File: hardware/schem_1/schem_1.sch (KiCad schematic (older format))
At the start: 37 parts, among them J1 OV7670_Conn_01x24_MountingPin, J2 Micro_SD_Card, J3 FRONT_PCB_CONNECTOR, J4 BG300-04-X-X-A_REVC, J6 BACK_PCB_CONNECTOR, SW1 BTN_BOOT, SW2 ESP32_RESET, U1 ESP32-WROVER-E-JC

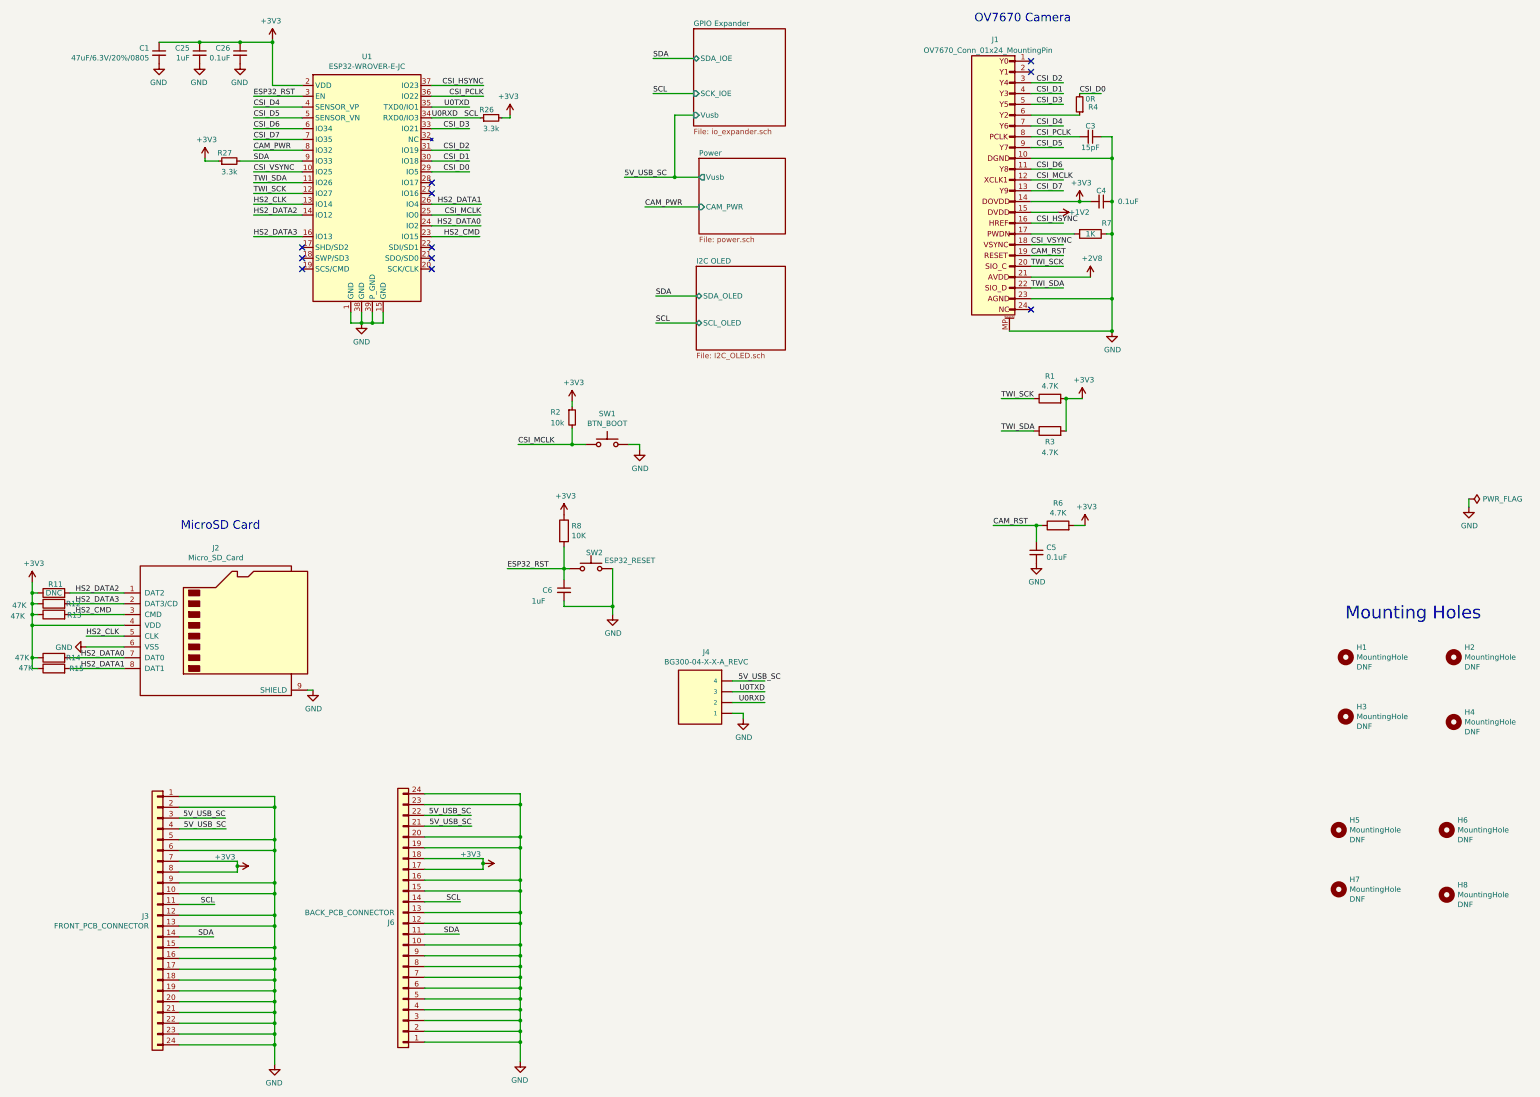
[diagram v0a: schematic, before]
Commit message: move old production stuff to new folder. start pcb spin 2: add test points (smd and pads). add third diode as currently disconnected USB can not be detected. increase LED resistor values are too bright. improve OLED footprint (to accomodate inaccuracies in drawing).
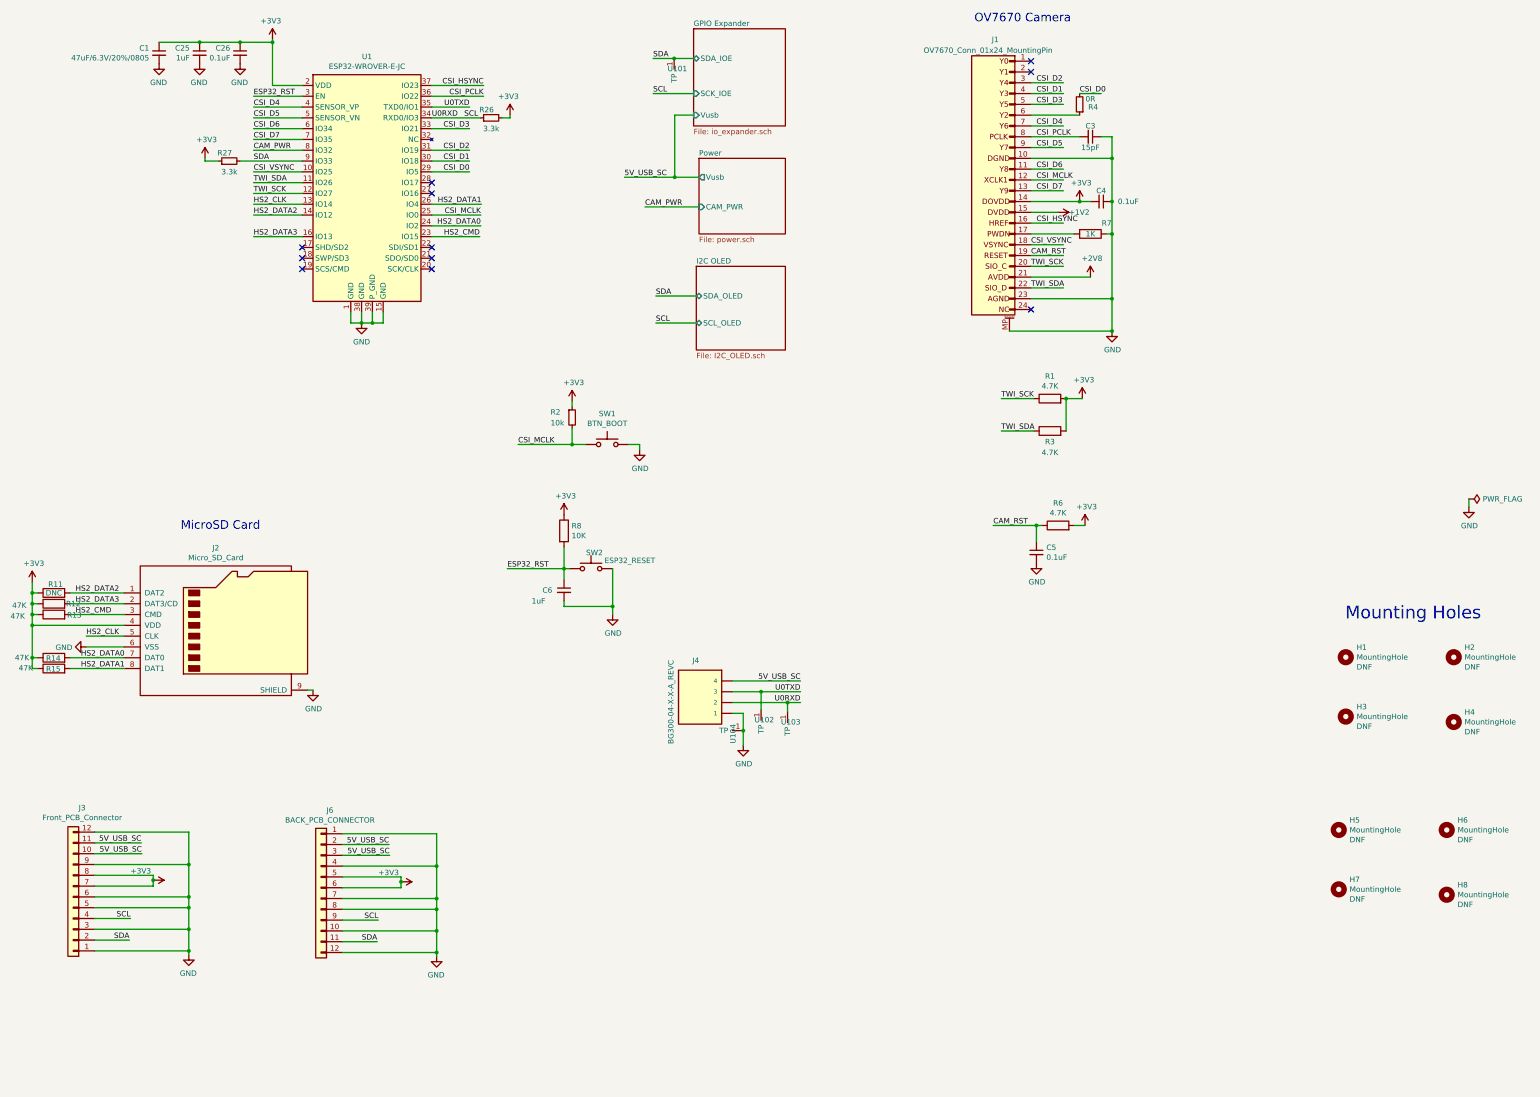
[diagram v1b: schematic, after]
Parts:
- removed J3: FRONT_PCB_CONNECTOR, Connector_FFC-FPC:TE_2-1734839-4_1x24-1MP_P0.5mm_Horizontal, symbol Connector_Generic:Conn_01x24
- removed J6: BACK_PCB_CONNECTOR, Connector_FFC-FPC:TE_2-1734839-4_1x24-1MP_P0.5mm_Horizontal, symbol Connector_Generic:Conn_01x24
- added J3: Front_PCB_Connector, Connector_Hirose:Hirose_DF3EA-12P-2H_1x12-1MP_P2.00mm_Horizontal, symbol Connector_Generic:Conn_01x12
- added J6: BACK_PCB_CONNECTOR, Connector_Hirose:Hirose_DF3EA-12P-2H_1x12-1MP_P2.00mm_Horizontal, symbol Connector_Generic:Conn_01x12
- added U101, U102, U103, U104: 0805_TEST_POINT, Digikey:PC_TEST_POINT_SMD, symbol jclib:0805_TEST_POINT
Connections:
- wire segments 218 -> 176

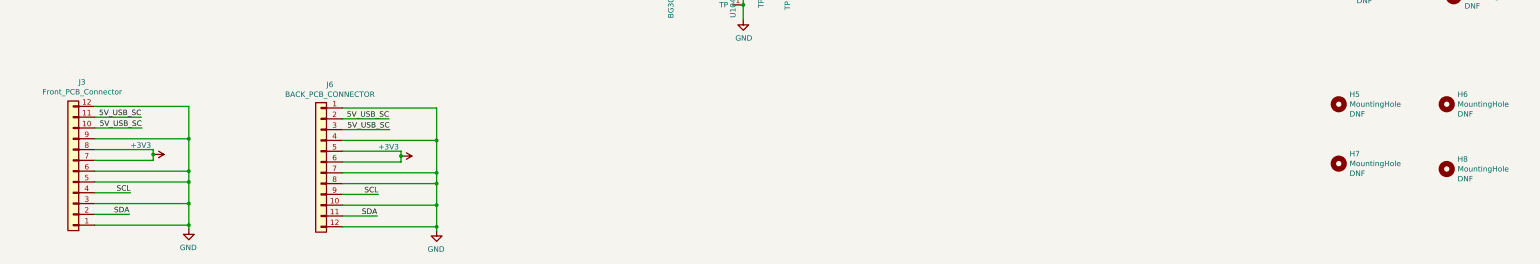
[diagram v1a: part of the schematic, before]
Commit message: make board on breadboard for easier debugging and fixing. will start writing f/w on this board
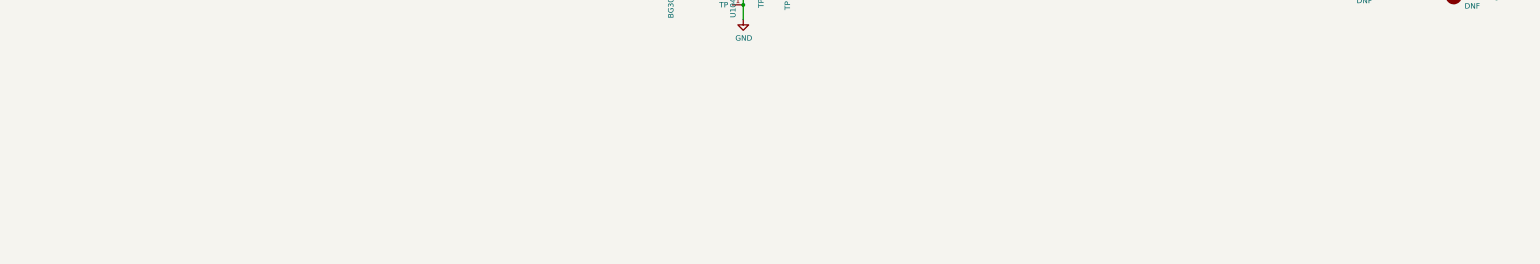
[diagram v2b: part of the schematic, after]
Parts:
- removed H5, H6, H7, H8: MountingHole, MountingHole:MountingHole_2mm, symbol Mechanical:MountingHole
- removed J3: Front_PCB_Connector, Connector_Hirose:Hirose_DF3EA-12P-2H_1x12-1MP_P2.00mm_Horizontal, symbol Connector_Generic:Conn_01x12
- removed J6: BACK_PCB_CONNECTOR, Connector_Hirose:Hirose_DF3EA-12P-2H_1x12-1MP_P2.00mm_Horizontal, symbol Connector_Generic:Conn_01x12
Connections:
- wire segments 176 -> 136
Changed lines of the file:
@@
 Text Label 6335 2300 0    50   ~ 0
 5V_USB_SC
-Text Label 1865 8565 2    50   ~ 0
-5V_USB_SC
-Wire Wire Line
-	1430 8465 1860 8465
-Text Label 1860 8465 2    50   ~ 0
-5V_USB_SC
-Text Label 1750 9365 2    50   ~ 0
-SDA
-Text Label 1760 9165 2    50   ~ 0
-SCL
-$Comp
-L power:GND #PWR0106
-U 1 1 60E565E8
-P 2300 9500
-F 0 "#PWR0106" H 2300 9250 50  0001 C CNN
-F 1 "GND" H 2305 9327 50  0000 C CNN
-F 2 "" H 2300 9500 50  0001 C CNN
-F 3 "" H 2300 9500 50  0001 C CNN
-	1    2300 9500
-	-1   0    0    -1
-$EndComp
-Wire Wire Line
-	1430 8565 1865 8565
 Text Label 4850 1750 0    50   ~ 0
 SCL
@@
 	3350 1650 2900 1650
 $Comp
-L Mechanical:MountingHole H5
-U 1 1 612159A3
-P 12950 8345
-F 0 "H5" H 13050 8436 50  0000 L CNN
-F 1 "MountingHole" H 13050 8345 50  0000 L CNN
-F 2 "MountingHole:MountingHole_2mm" H 12950 8345 50  0001 C CNN
-F 3 "~" H 12950 8345 50  0001 C CNN
-F 4 "DNF" H 13050 8254 50  0000 L CNN "DNF"
-	1    12950 8345
-	1    0    0    -1
-$EndComp
-$Comp
-L Mechanical:MountingHole H6
-U 1 1 61215EE2
-P 13950 8345
-F 0 "H6" H 14050 8436 50  0000 L CNN
-F 1 "MountingHole" H 14050 8345 50  0000 L CNN
-F 2 "MountingHole:MountingHole_2mm" H 13950 8345 50  0001 C CNN
-F 3 "~" H 13950 8345 50  0001 C CNN
-F 4 "DNF" H 14050 8254 50  0000 L CNN "DNF"
-	1    13950 8345
-	1    0    0    -1
-$EndComp
-$Comp
-L Mechanical:MountingHole H7
-U 1 1 61215EED
-P 12950 8895
-F 0 "H7" H 13050 8986 50  0000 L CNN
-F 1 "MountingHole" H 13050 8895 50  0000 L CNN
-F 2 "MountingHole:MountingHole_2mm" H 12950 8895 50  0001 C CNN
-F 3 "~" H 12950 8895 50  0001 C CNN
-F 4 "DNF" H 13050 8804 50  0000 L CNN "DNF"
-	1    12950 8895
-	1    0    0    -1
-$EndComp
-$Comp
-L Mechanical:MountingHole H8
-U 1 1 61215EF8
-P 13950 8945
-F 0 "H8" H 14050 9036 50  0000 L CNN
-F 1 "MountingHole" H 14050 8945 50  0000 L CNN
-F 2 "MountingHole:MountingHole_2mm" H 13950 8945 50  0001 C CNN
-F 3 "~" H 13950 8945 50  0001 C CNN
-F 4 "DNF" H 14050 8854 50  0000 L CNN "DNF"
-	1    13950 8945
-	1    0    0    -1
-$EndComp
-$Comp
 L jclib:ESP32-WROVER-E-JC U1
 U 1 1 616E7DD7
@@
 Wire Wire Line
 	4550 2850 4995 2850
-Wire Wire Line
-	1760 9165 1430 9165
-Wire Wire Line
-	1430 9365 1750 9365
 Wire Wire Line
 	6800 2300 6335 2300
@@
 	0    1    1    0
 $EndComp
-$Comp
-L Connector_Generic:Conn_01x12 J3
-U 1 1 612D81CF
-P 1230 8965
-F 0 "J3" H 1148 8140 50  0000 C CNN
-F 1 "Front_PCB_Connector" H 1148 8231 50  0000 C CNN
-F 2 "Connector_Hirose:Hirose_DF3EA-12P-2H_1x12-1MP_P2.00mm_Horizontal" H 1230 8965 50  0001 C CNN
-F 3 "~" H 1230 8965 50  0001 C CNN
-	1    1230 8965
-	-1   0    0    1
-$EndComp
-Wire Wire Line
-	1970 8810 1970 8765
-Connection ~ 1970 8810
-Wire Wire Line
-	1970 8865 1970 8810
-Wire Wire Line
-	1430 8865 1970 8865
-$Comp
-L power:+3V3 #PWR0105
-U 1 1 60D9B54C
-P 1970 8810
-F 0 "#PWR0105" H 1970 8660 50  0001 C CNN
-F 1 "+3V3" V 2055 8695 50  0000 C CNN
-F 2 "" H 1970 8810 50  0001 C CNN
-F 3 "" H 1970 8810 50  0001 C CNN
-	1    1970 8810
-	0    1    -1   0
-$EndComp
-Wire Wire Line
-	1430 8765 1970 8765
-Wire Wire Line
-	1430 8365 2300 8365
-Wire Wire Line
-	2300 8365 2300 8665
-Wire Wire Line
-	1430 8665 2300 8665
-Connection ~ 2300 8665
-Wire Wire Line
-	2300 8665 2300 8965
-Wire Wire Line
-	1430 8965 2300 8965
-Connection ~ 2300 8965
-Wire Wire Line
-	2300 8965 2300 9065
-Wire Wire Line
-	1430 9065 2300 9065
-Connection ~ 2300 9065
-Wire Wire Line
-	2300 9065 2300 9265
-Wire Wire Line
-	1430 9265 2300 9265
-Connection ~ 2300 9265
-Wire Wire Line
-	2300 9265 2300 9465
-Wire Wire Line
-	1430 9465 2300 9465
-Connection ~ 2300 9465
-Wire Wire Line
-	2300 9465 2300 9500
-Text Label 4160 8580 2    50   ~ 0
-5V_USB_SC
-Wire Wire Line
-	3725 8480 4155 8480
-Text Label 4155 8480 2    50   ~ 0
-5V_USB_SC
-Text Label 4045 9380 2    50   ~ 0
-SDA
-Text Label 4055 9180 2    50   ~ 0
-SCL
-$Comp
-L power:GND #PWR0107
-U 1 1 613BBE4D
-P 4595 9515
-F 0 "#PWR0107" H 4595 9265 50  0001 C CNN
-F 1 "GND" H 4600 9342 50  0000 C CNN
-F 2 "" H 4595 9515 50  0001 C CNN
-F 3 "" H 4595 9515 50  0001 C CNN
-	1    4595 9515
-	-1   0    0    -1
-$EndComp
-Wire Wire Line
-	3725 8580 4160 8580
-Wire Wire Line
-	4055 9180 3725 9180
-Wire Wire Line
-	3725 9380 4045 9380
-$Comp
-L Connector_Generic:Conn_01x12 J6
-U 1 1 613BBE5A
-P 3525 8880
-F 0 "J6" H 3443 9597 50  0000 C CNN
-F 1 "BACK_PCB_CONNECTOR" H 3443 9506 50  0000 C CNN
-F 2 "Connector_Hirose:Hirose_DF3EA-12P-2H_1x12-1MP_P2.00mm_Horizontal" H 3525 8880 50  0001 C CNN
-F 3 "~" H 3525 8880 50  0001 C CNN
-	1    3525 8880
-	-1   0    0    -1
-$EndComp
-Wire Wire Line
-	4265 8825 4265 8780
-Connection ~ 4265 8825
-Wire Wire Line
-	4265 8880 4265 8825
-Wire Wire Line
-	3725 8880 4265 8880
-$Comp
-L power:+3V3 #PWR0108
-U 1 1 613BBE68
-P 4265 8825
-F 0 "#PWR0108" H 4265 8675 50  0001 C CNN
-F 1 "+3V3" V 4350 8710 50  0000 C CNN
-F 2 "" H 4265 8825 50  0001 C CNN
-F 3 "" H 4265 8825 50  0001 C CNN
-	1    4265 8825
-	0    1    -1   0
-$EndComp
-Wire Wire Line
-	3725 8780 4265 8780
-Wire Wire Line
-	3725 8380 4595 8380
-Wire Wire Line
-	4595 8380 4595 8680
-Wire Wire Line
-	3725 8680 4595 8680
-Connection ~ 4595 8680
-Wire Wire Line
-	4595 8680 4595 8980
-Wire Wire Line
-	3725 8980 4595 8980
-Connection ~ 4595 8980
-Wire Wire Line
-	4595 8980 4595 9080
-Wire Wire Line
-	3725 9080 4595 9080
-Connection ~ 4595 9080
-Wire Wire Line
-	4595 9080 4595 9280
-Wire Wire Line
-	3725 9280 4595 9280
-Connection ~ 4595 9280
-Wire Wire Line
-	4595 9280 4595 9480
-Wire Wire Line
-	3725 9480 4595 9480
-Connection ~ 4595 9480
-Wire Wire Line
-	4595 9480 4595 9515
 Wire Wire Line
 	7335 7065 7600 7065
